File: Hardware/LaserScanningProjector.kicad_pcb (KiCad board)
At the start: 2 copper layers, 84.8 x 89.9 mm, 78 parts, among them J1 5V_IN, J10 MOTOR_Y, J11 LASER, J2 SWD, J3 UART, J4 USB_B, J5 LCD, J6 Micro_SD_Card_Det, J7 AUX, J8 HEADPHONES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

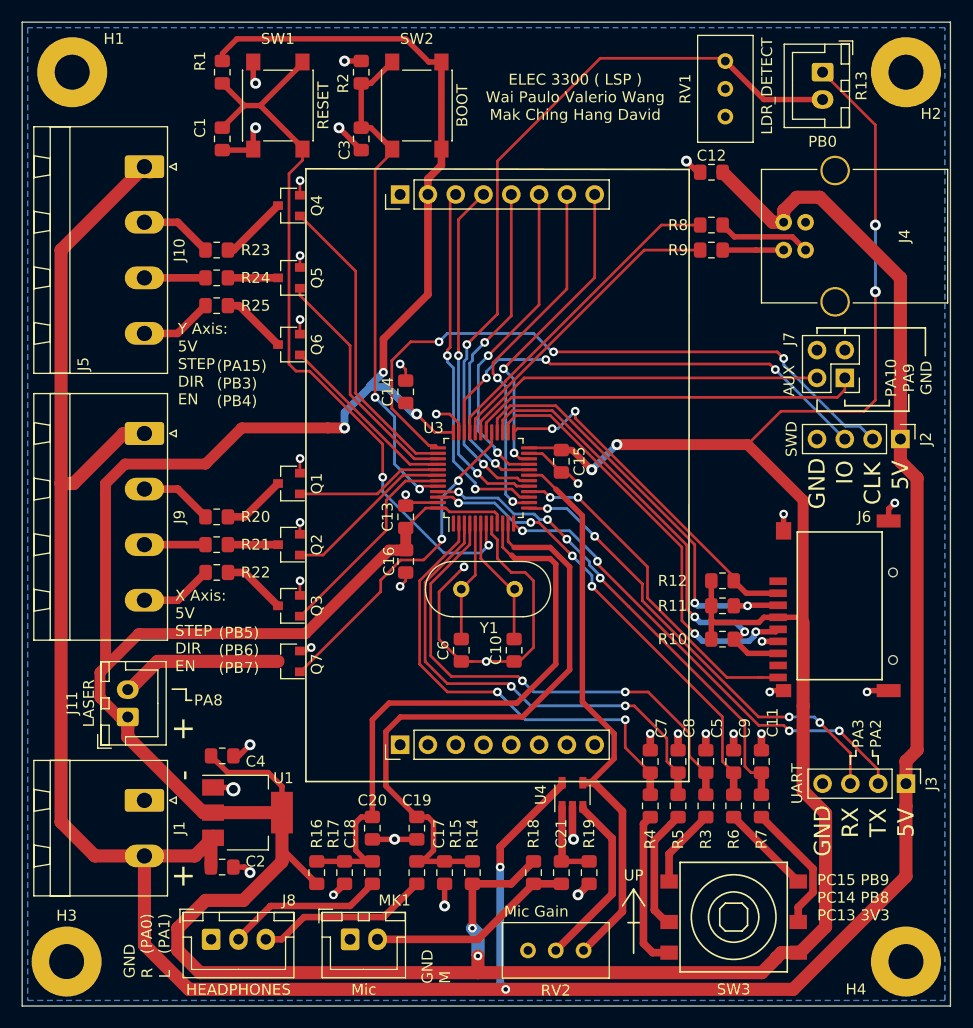
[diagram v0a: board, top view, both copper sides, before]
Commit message: Minor changes to hardware
- Changed laser power supply from 3v3 to 5v
   - 5v for more flexibility in laser diode selection
- Bumped revision number to v1.0
- Added version number to PCB
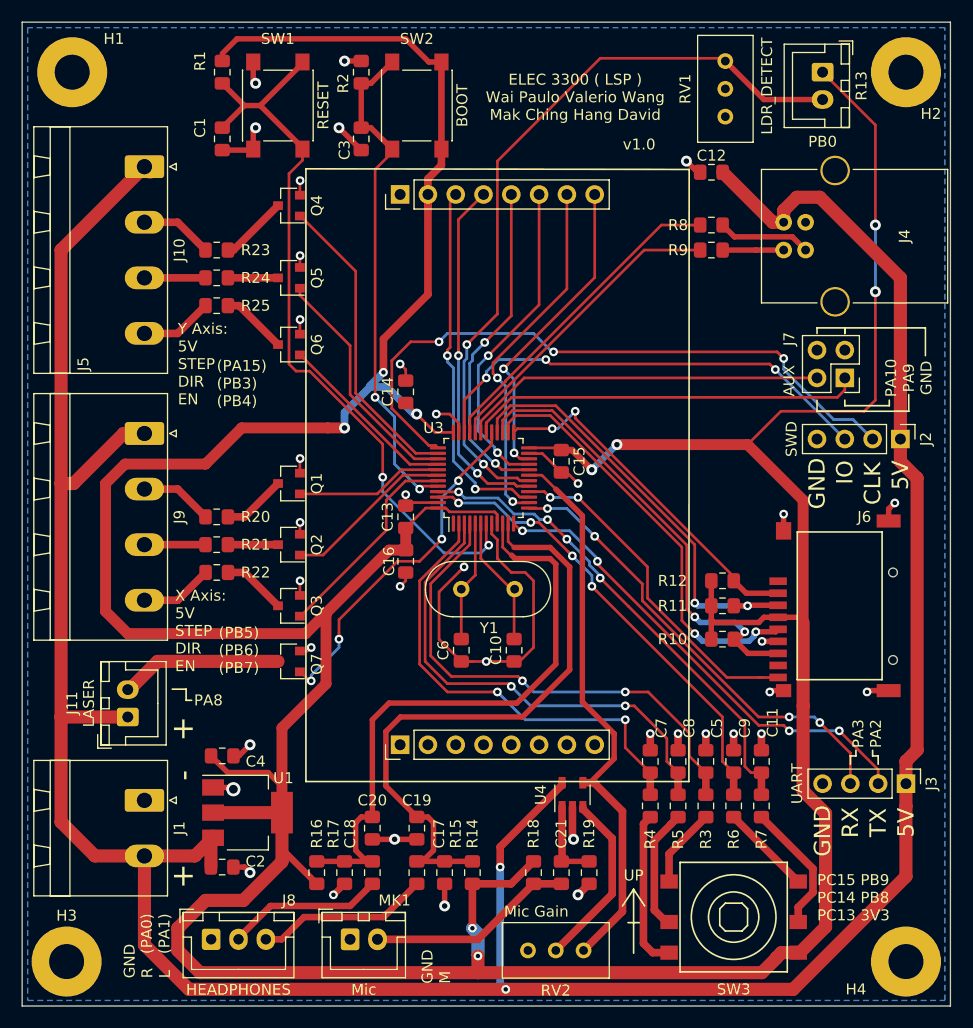
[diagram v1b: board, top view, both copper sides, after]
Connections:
- J11 pad 1: +3V3 -> +5V
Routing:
- net +5V: track 275.7 -> 281.8 mm
- net +3V3: track 423.0 -> 418.6 mm
- net LASER_PWM: track 30.4 -> 32.1 mm, vias 2 -> 4
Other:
- board text added: "v1.0"
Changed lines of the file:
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@@
   (general
     (thickness 1.6)
-    (drawings 330)
-    (tracks 823)
+    (drawings 331)
+    (tracks 827)
     (zones 0)
     (modules 78)
@@
       (net 46 "Net-(J11-Pad2)"))
     (pad 1 thru_hole roundrect (at 0 0 90) (size 1.7 2) (drill 1) (layers *.Cu *.Mask) (roundrect_rratio 0.147059)
-      (net 5 +3V3))
+      (net 3 +5V))
     (model ${KISYS3DMOD}/Connector_JST.3dshapes/JST_XH_B2B-XH-A_1x02_P2.50mm_Vertical.wrl
       (at (xyz 0 0 0))
@@
     )
   )
+  (gr_text v1.0 (at 121.412 35.56) (layer F.SilkS)
+    (effects (font (size 1 1) (thickness 0.15)))
+  )
   (gr_line (start 96.042027 83.883577) (end 96.30157 83.624065) (layer B.SilkS) (width 0.08))
   (gr_line (start 95.782376 83.624065) (end 96.042027 83.883577) (layer B.SilkS) (width 0.08))
@@
   (segment (start 108.712 101.6) (end 108.712 112.268) (width 0.7) (layer B.Cu) (net 3))
   (segment (start 68.58 45.212) (end 76.2 37.592) (width 1.2) (layer F.Cu) (net 3))
-  (segment (start 68.58 97.488) (end 68.58 66.548) (width 1.2) (layer F.Cu) (net 3))
   (segment (start 76.2 100.584) (end 71.676 100.584) (width 1.2) (layer F.Cu) (net 3))
   (segment (start 71.676 100.584) (end 68.58 97.488) (width 1.2) (layer F.Cu) (net 3))
@@
   (segment (start 133.613 42.672) (end 129.041 38.1) (width 1.2) (layer F.Cu) (net 3))
   (segment (start 134.62 42.672) (end 133.613 42.672) (width 1.2) (layer F.Cu) (net 3))
+  (segment (start 68.58 87.884) (end 74.676 87.884) (width 1.2) (layer F.Cu) (net 3))
+  (segment (start 68.58 87.884) (end 68.58 66.548) (width 1.2) (layer F.Cu) (net 3))
+  (segment (start 68.58 97.488) (end 68.58 87.884) (width 1.2) (layer F.Cu) (net 3))
   (segment (start 96.885 29.981) (end 98.842 28.024) (width 0.5) (layer F.Cu) (net 4))
   (segment (start 96.012 29.981) (end 96.885 29.981) (width 0.5) (layer F.Cu) (net 4))
@@
   (segment (start 106.68 111.252) (end 132.626 111.252) (width 1.2) (layer F.Cu) (net 5))
   (segment (start 132.626 111.252) (end 133.948 109.93) (width 1.2) (layer F.Cu) (net 5))
-  (segment (start 74.676 88.834) (end 74.676 87.884) (width 1.2) (layer F.Cu) (net 5))
-  (segment (start 82.4685 96.6255) (end 81.578498 96.6255) (width 1.2) (layer F.Cu) (net 5))
-  (segment (start 74.676 89.723002) (end 74.676 88.834) (width 1.2) (layer F.Cu) (net 5))
-  (segment (start 81.578498 96.6255) (end 74.676 89.723002) (width 1.2) (layer F.Cu) (net 5))
   (segment (start 138.448011 96.694013) (end 136.398 94.644002) (width 1.2) (layer F.Cu) (net 5))
   (segment (start 138.448011 107.071989) (end 138.448011 96.694013) (width 1.2) (layer F.Cu) (net 5))
@@
   (segment (start 104.438 61.8775) (end 102.7625 61.8775) (width 0.25) (layer F.Cu) (net 5))
   (segment (start 100.076 72.635) (end 100.076 70.621) (width 1) (layer F.Cu) (net 5))
-  (segment (start 99.276 72.635) (end 100.076 72.635) (width 1) (layer F.Cu) (net 5))
-  (segment (start 98.557002 72.635) (end 99.276 72.635) (width 1) (layer F.Cu) (net 5))
-  (segment (start 90.928002 80.264) (end 98.557002 72.635) (width 1) (layer F.Cu) (net 5))
-  (segment (start 73.914 87.884) (end 72.136 86.106) (width 1) (layer F.Cu) (net 5))
-  (segment (start 72.136 86.106) (end 72.136 83.82) (width 1) (layer F.Cu) (net 5))
-  (segment (start 74.676 87.884) (end 73.914 87.884) (width 1) (layer F.Cu) (net 5))
-  (segment (start 75.692 80.264) (end 90.928002 80.264) (width 1) (layer F.Cu) (net 5))
-  (segment (start 72.644 83.312) (end 72.644 67.391255) (width 1) (layer F.Cu) (net 5))
-  (segment (start 72.644 83.312) (end 75.692 80.264) (width 1) (layer F.Cu) (net 5))
-  (segment (start 72.136 83.82) (end 72.644 83.312) (width 1) (layer F.Cu) (net 5))
-  (segment (start 72.644 67.391255) (end 72.644 66.548) (width 1) (layer F.Cu) (net 5))
-  (segment (start 72.644 66.548) (end 74.422 64.77) (width 1) (layer F.Cu) (net 5))
-  (segment (start 74.422 64.77) (end 81.788 64.77) (width 1) (layer F.Cu) (net 5))
-  (segment (start 81.788 64.77) (end 85.09 61.468) (width 1) (layer F.Cu) (net 5))
-  (segment (start 85.09 61.468) (end 92.964 61.468) (width 1) (layer F.Cu) (net 5))
-  (segment (start 92.964 61.468) (end 94.488 61.468) (width 1) (layer F.Cu) (net 5))
   (via (at 94.488 61.468) (size 1) (drill 0.5) (layers F.Cu B.Cu) (net 5))
   (segment (start 96.825999 57.723999) (end 98.363999 57.723999) (width 0.7) (layer B.Cu) (net 5))
@@
   (segment (start 132.812 78.774) (end 132.338 79.248) (width 0.5) (layer F.Cu) (net 5))
   (segment (start 83.312 27.931) (end 83.312 27.256) (width 0.25) (layer F.Cu) (net 5))
+  (segment (start 85.09 61.468) (end 92.964 61.468) (width 1) (layer F.Cu) (net 5))
+  (segment (start 81.788 64.77) (end 85.09 61.468) (width 1) (layer F.Cu) (net 5))
+  (segment (start 74.422 64.77) (end 81.788 64.77) (width 1) (layer F.Cu) (net 5))
+  (segment (start 92.964 61.468) (end 94.488 61.468) (width 1) (layer F.Cu) (net 5))
+  (segment (start 100.076 72.635) (end 98.557002 72.635) (width 1) (layer F.Cu) (net 5))
+  (segment (start 90.928002 80.264) (end 74.676 80.264) (width 1) (layer F.Cu) (net 5))
+  (segment (start 74.676 80.264) (end 72.644 78.232) (width 1) (layer F.Cu) (net 5))
+  (segment (start 72.644 66.548) (end 74.422 64.77) (width 1) (layer F.Cu) (net 5))
+  (segment (start 72.644 78.232) (end 72.644 66.548) (width 1) (layer F.Cu) (net 5))
+  (segment (start 98.557002 72.635) (end 92.708001 78.484001) (width 1) (layer F.Cu) (net 5))
+  (segment (start 92.708001 78.484001) (end 90.928002 80.264) (width 1) (layer F.Cu) (net 5))
+  (segment (start 88.7685 96.6255) (end 88.7685 88.881502) (width 1) (layer F.Cu) (net 5))
+  (segment (start 88.7685 88.881502) (end 92.794001 84.856001) (width 1) (layer F.Cu) (net 5))
+  (segment (start 92.794001 78.570001) (end 92.708001 78.484001) (width 1) (layer F.Cu) (net 5))
+  (segment (start 92.794001 84.856001) (end 92.794001 78.570001) (width 1) (layer F.Cu) (net 5))
   (segment (start 127.508 92.973) (end 127.508 94.987) (width 0.7) (layer F.Cu) (net 6))
   (via (at 120.142 85.598) (size 0.8) (drill 0.4) (layers F.Cu B.Cu) (net 6))
@@
   (segment (start 111.76 52.832) (end 113.445306 54.517306) (width 0.25) (layer B.Cu) (net 20))
   (segment (start 113.445306 54.517306) (end 113.589522 54.517306) (width 0.25) (layer B.Cu) (net 20))
-  (segment (start 142.748 62.484) (end 141.572999 61.308999) (width 0.25) (layer B.Cu) (net 20))
   (segment (start 113.589522 54.517306) (end 134.019306 54.517306) (width 0.25) (layer F.Cu) (net 20))
-  (segment (start 134.62 55.683685) (end 134.62 55.118) (width 0.25) (layer B.Cu) (net 20))
   (via (at 134.62 55.118) (size 0.8) (drill 0.4) (layers F.Cu B.Cu) (net 20))
-  (segment (start 140.245314 61.308999) (end 134.62 55.683685) (width 0.25) (layer B.Cu) (net 20))
   (segment (start 134.019306 54.517306) (end 134.220001 54.718001) (width 0.25) (layer F.Cu) (net 20))
   (segment (start 134.220001 54.718001) (end 134.62 55.118) (width 0.25) (layer F.Cu) (net 20))
-  (segment (start 141.572999 61.308999) (end 140.245314 61.308999) (width 0.25) (layer B.Cu) (net 20))
+  (segment (start 139.192 60.706) (end 134.62 56.134) (width 0.25) (layer B.Cu) (net 20))
+  (segment (start 142.748 62.484) (end 140.97 60.706) (width 0.25) (layer B.Cu) (net 20))
+  (segment (start 134.62 56.134) (end 134.62 55.118) (width 0.25) (layer B.Cu) (net 20))
+  (segment (start 140.97 60.706) (end 139.192 60.706) (width 0.25) (layer B.Cu) (net 20))
   (via (at 137.922 88.392) (size 0.8) (drill 0.4) (layers F.Cu B.Cu) (net 21))
   (segment (start 140.716 93.98) (end 140.716 91.186) (width 0.25) (layer F.Cu) (net 21))
@@
   (segment (start 107.938 61.8775) (end 107.938 63.004) (width 0.25) (layer F.Cu) (net 59))
   (segment (start 107.938 63.004) (end 104.902 66.04) (width 0.25) (layer F.Cu) (net 59))
-  (segment (start 97.79 76.422) (end 97.79 75.38281) (width 0.25) (layer F.Cu) (net 59))
-  (segment (start 90.458 83.754) (end 97.79 76.422) (width 0.25) (layer F.Cu) (net 59))
+  (segment (start 91.285996 84.581996) (end 91.44 84.581996) (width 0.25) (layer F.Cu) (net 59))
+  (via (at 91.44 84.581996) (size 0.8) (drill 0.4) (layers F.Cu B.Cu) (net 59))
   (segment (start 90.408 83.754) (end 90.458 83.754) (width 0.25) (layer F.Cu) (net 59))
-  (segment (start 97.79 75.38281) (end 99.6378 73.53501) (width 0.25) (layer F.Cu) (net 59))
-  (segment (start 99.6378 73.53501) (end 101.72499 73.53501) (width 0.25) (layer F.Cu) (net 59))
-  (segment (start 101.72499 73.53501) (end 103.378 71.882) (width 0.25) (layer F.Cu) (net 59))
-  (segment (start 103.378 71.882) (end 103.378 71.628) (width 0.25) (layer F.Cu) (net 59))
+  (segment (start 90.458 83.754) (end 91.285996 84.581996) (width 0.25) (layer F.Cu) (net 59))
+  (segment (start 93.98 80.206315) (end 93.98 80.772) (width 0.25) (layer F.Cu) (net 59))
+  (via (at 93.98 80.772) (size 0.8) (drill 0.4) (layers F.Cu B.Cu) (net 59))
+  (segment (start 101.346 73.66) (end 99.314 73.66) (width 0.25) (layer F.Cu) (net 59))
+  (segment (start 103.378 71.628) (end 101.346 73.66) (width 0.25) (layer F.Cu) (net 59))
+  (segment (start 93.98 78.994) (end 93.98 80.206315) (width 0.25) (layer F.Cu) (net 59))
+  (segment (start 99.314 73.66) (end 93.98 78.994) (width 0.25) (layer F.Cu) (net 59))
+  (segment (start 93.98 81.533998) (end 93.98 81.337685) (width 0.25) (layer B.Cu) (net 59))
+  (segment (start 91.44 84.581996) (end 91.44 84.073998) (width 0.25) (layer B.Cu) (net 59))
+  (segment (start 93.98 81.337685) (end 93.98 80.772) (width 0.25) (layer B.Cu) (net 59))
+  (segment (start 91.44 84.073998) (end 93.98 81.533998) (width 0.25) (layer B.Cu) (net 59))
   (segment (start 127.508 97.037) (end 124.977 99.568) (width 0.7) (layer F.Cu) (net 60))
   (segment (start 124.968 99.568) (end 124.148 100.388) (width 0.7) (layer F.Cu) (net 60))

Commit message: Fix typo in silkscreen; Display BL -> PB11
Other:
- board text added: "PB11"
- board text removed: "PA11"
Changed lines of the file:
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@@
     (effects (font (size 1 1) (thickness 0.15)) (justify left))
   )
-  (gr_text PA11 (at 117.348 36.068 90) (layer B.SilkS)
+  (gr_text PB11 (at 117.348 36.068 90) (layer B.SilkS)
     (effects (font (size 1 1) (thickness 0.15)) (justify mirror))
   )

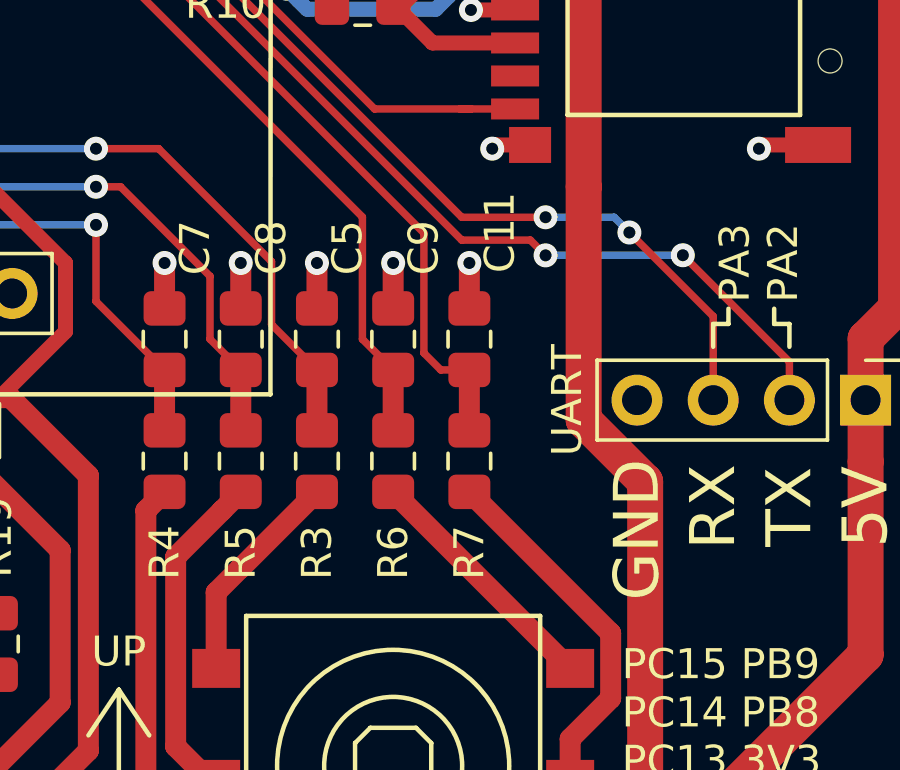
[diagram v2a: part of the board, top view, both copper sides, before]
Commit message: Swap center and right pins on 5 dir nav switch
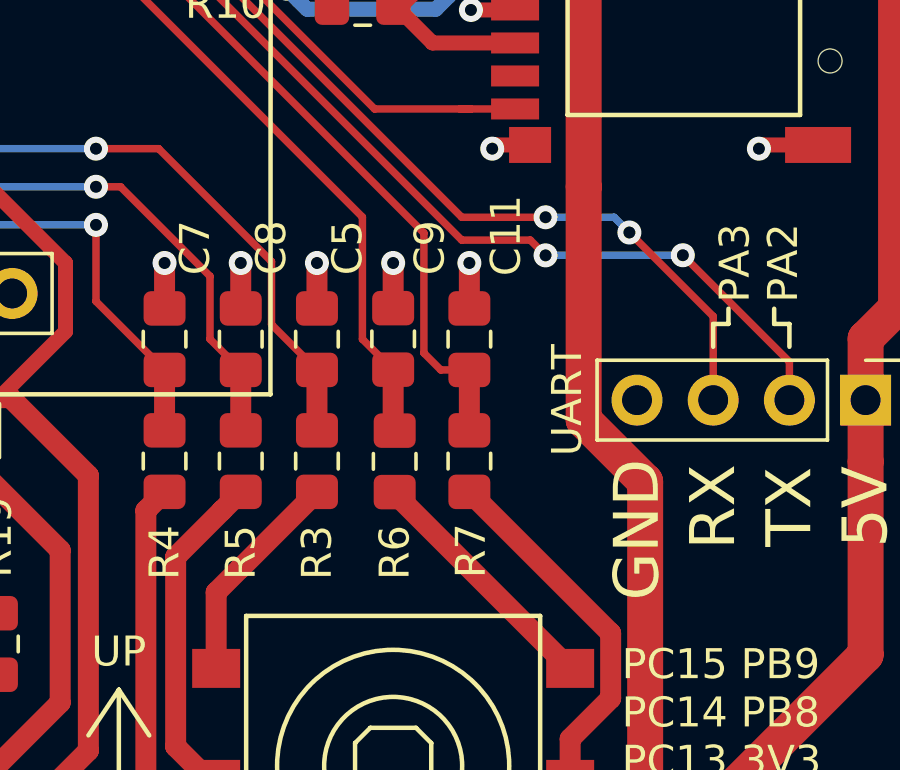
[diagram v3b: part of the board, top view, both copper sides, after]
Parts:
- moved R6 0.05 mm to (130.1, 96.0)
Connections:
- C11 pad 1: IN_CENTER -> IN_RIGHT
- C9 pad 1: IN_RIGHT -> IN_CENTER
- R6 pad 1: IN_RIGHT -> IN_CENTER
- R7 pad 1: IN_CENTER -> IN_RIGHT
- U3 pad 45: IN_CENTER -> IN_RIGHT
- U3 pad 46: IN_RIGHT -> IN_CENTER
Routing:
- net IN_RIGHT: track 43.3 -> 44.4 mm
- net IN_CENTER: track 44.4 -> 43.3 mm
